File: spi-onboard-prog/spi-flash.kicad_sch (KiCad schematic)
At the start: 4 parts, among them U1 SST25VF080B-50-4x-S2Ax, U3 74LS257

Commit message: layout work on onboard spi prog
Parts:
- added JP2: Jumper_3_Open, Connector_PinHeader_2.54mm:PinHeader_1x03_P2.54mm_Vertical, symbol Jumper:Jumper_3_Open
- added U4: 74LVC1G125, Package_TO_SOT_SMD:SOT-23-5_HandSoldering, symbol 74xGxx:74LVC1G125
- U1: footprint Package_SO:SOIC-8_5.3x5.3mm_P1.27mm -> Package_DIP:DIP-8_W7.62mm
- U3: value 74LS257 -> 74LVC257; footprint Package_SO:SOP-16_4.4x10.4mm_P1.27mm -> Package_SO:SOIC-16_3.9x9.9mm_P1.27mm; LCSC C2872319 -> C165622
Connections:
- net 3.3V: now also JP2.3 (B), U4.5 (VCC)
- net GND: now also U3.15 (OE), JP2.1 (A), U4.1, U4.3 (GND)
- net MISO2: now also U1.2 (SO), U4.2
- net USB_MISO: now also U4.4
- net at U3.1 (S): now also JP2.2 (C)

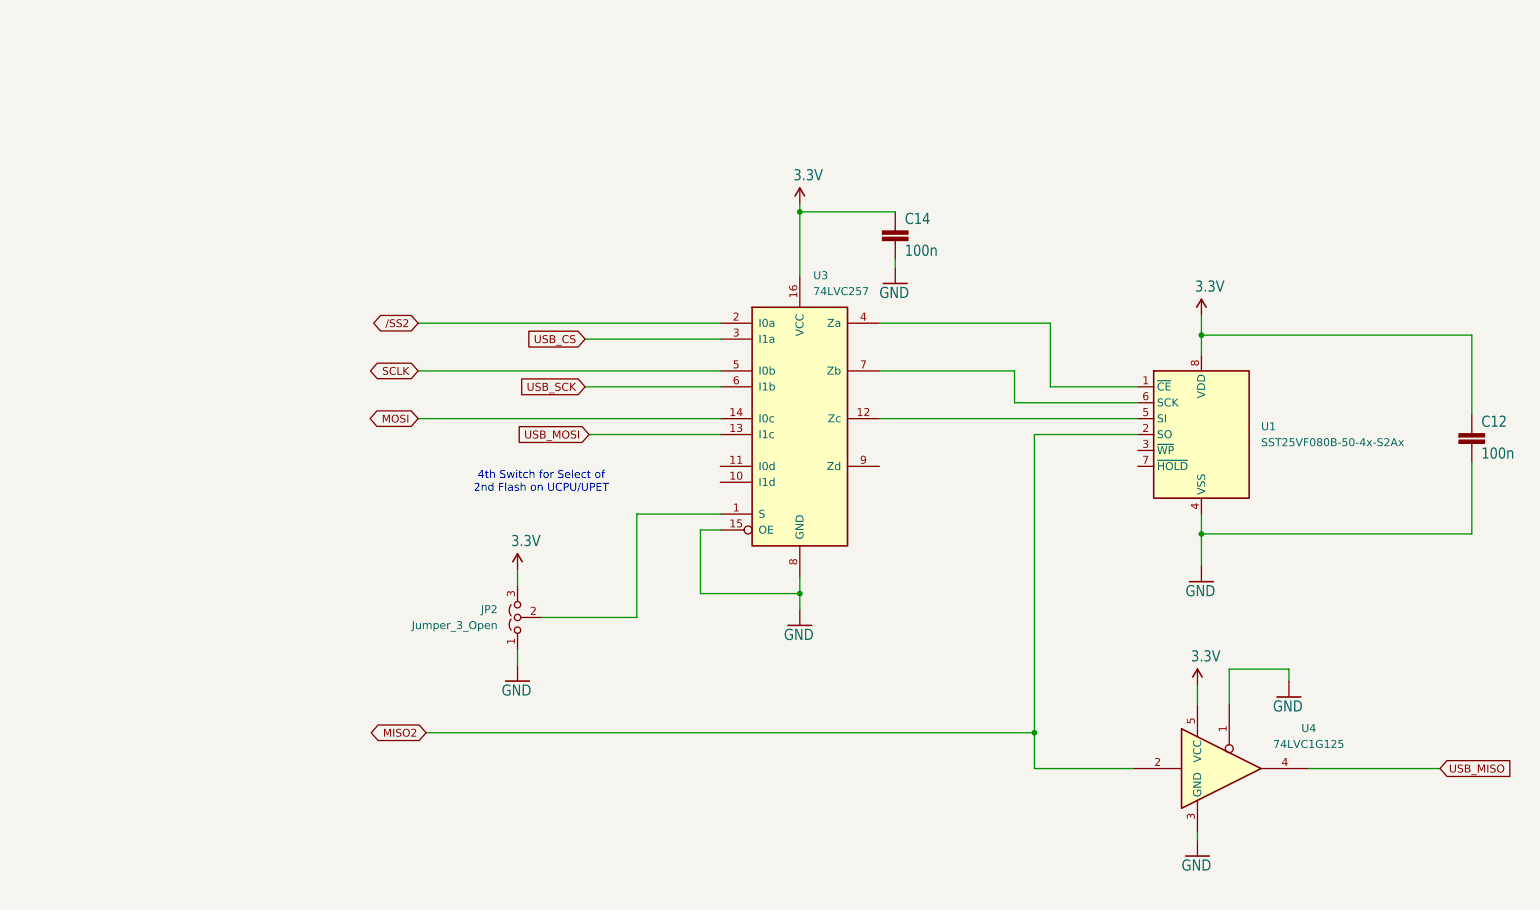
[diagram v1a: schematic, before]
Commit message: onboard prog on SPI10-3.3V
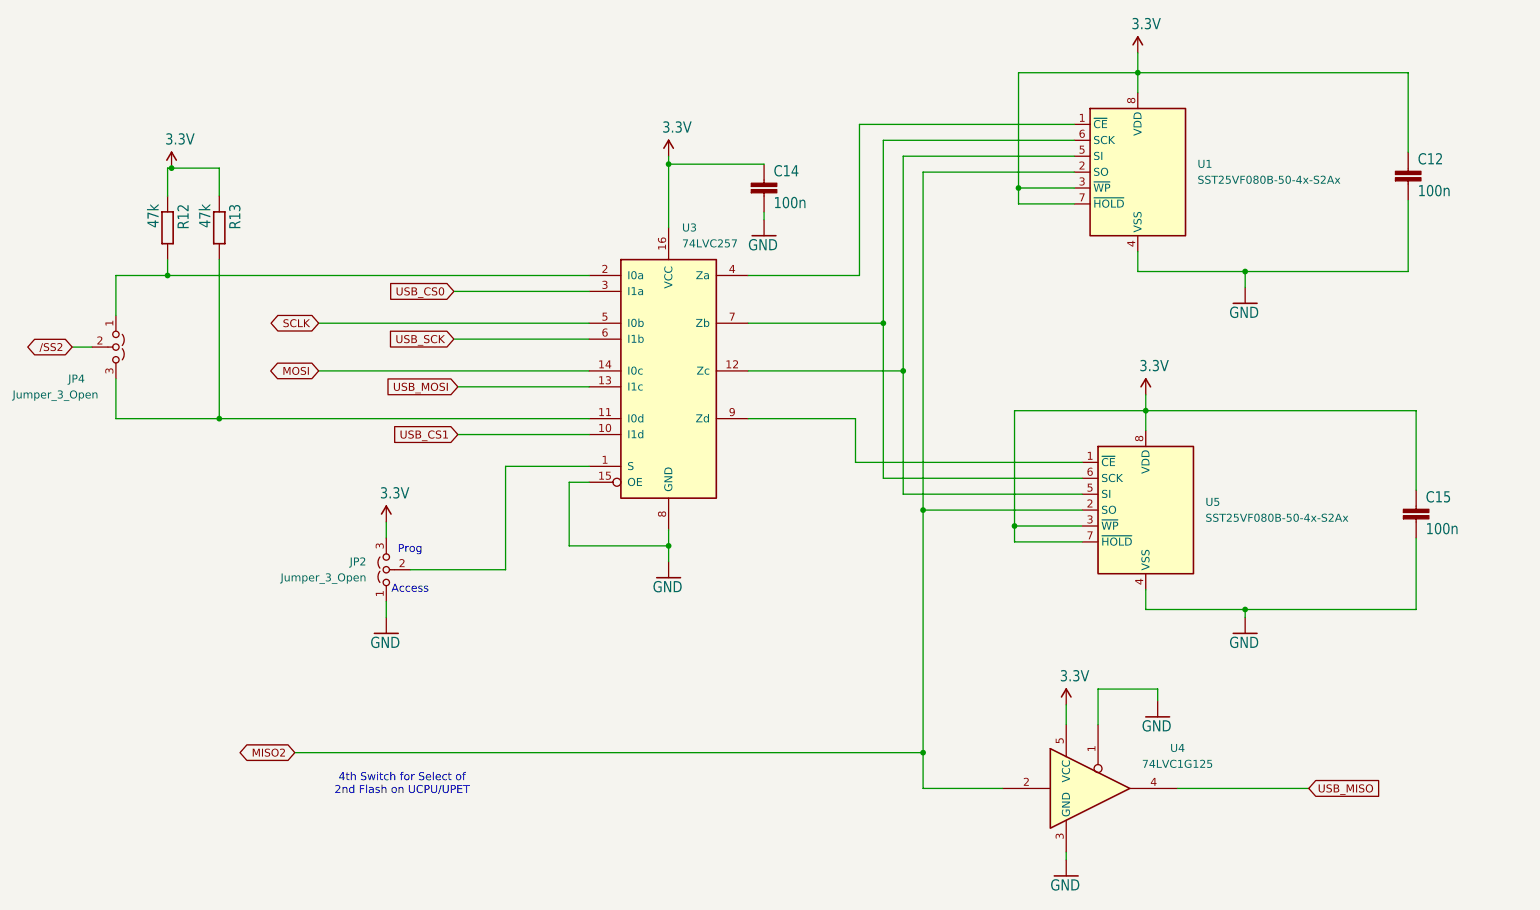
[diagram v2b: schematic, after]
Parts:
- added C15: 100n, Capacitor_SMD:C_0603_1608Metric_Pad1.08x0.95mm_HandSolder, symbol cbm_usb_v1-eagle-import:C-EU050-025X075
- added JP4: Jumper_3_Open, Connector_PinHeader_2.54mm:PinHeader_1x03_P2.54mm_Vertical, symbol Jumper:Jumper_3_Open
- added R12, R13: 47k, Resistor_SMD:R_0603_1608Metric_Pad0.98x0.95mm_HandSolder, symbol cbm_usb_v1-eagle-import:R-EU_0204/7
- added U5: SST25VF080B-50-4x-S2Ax, Package_SO:SOIC-8_5.3x6.2mm_P1.27mm, symbol Memory_Flash:SST25VF080B-50-4x-S2Ax
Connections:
- net /SS2: now also JP4.2 (C); no longer U3.2 (I0a)
- net 3.3V: now also U1.3 (~{WP}), U1.7 (~{HOLD}), C15.1, R12.1, R13.1, U5.3 (~{WP}), U5.7 (~{HOLD}), U5.8 (VDD)
- net GND: now also C15.2, U5.4 (VSS)
- net MISO2: now also U5.2 (SO)
- net USB_CS1: now reaches U3.10 (I1d)
- net at U3.11 (I0d): now also JP4.3 (B), R13.2
- net at U1.5 (SI), U3.12 (Zc): now also U5.5 (SI)
- net at U1.6 (SCK), U3.7 (Zb): now also U5.6 (SCK)
- net at U3.9 (Zd): now also U5.1 (~{CE})
- net USB_CS renamed USB_CS0
- new net: JP4.1 (A), R12.2, U3.2 (I0a)
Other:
- note added: "Access"
- note added: "Prog"
- moved on the sheet: C12, C14, JP2, U1, U3, U4

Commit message: onboard flash prog
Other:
- note removed: "4th Switch for Select of 2nd Flash on UCPU/UPET"
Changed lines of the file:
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@@
-		)
-	)
-	(text "4th Switch for Select of\n2nd Flash on UCPU/UPET"
-		(exclude_from_sim no)
-		(at 81.28 147.32 0)
-		(effects
-			(font
-				(size 1.27 1.27)
-			)
 		)
 	)
